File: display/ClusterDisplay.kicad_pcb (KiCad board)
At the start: 4 copper layers, 115.6 x 106 mm, 98 parts, among them J1 Verdin iMX95 Hexa 8GB WB IT, J10 RTC coin cell, J2 Phoenix MKDS 1,5/3-5,08 power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, J3 Molex KK-254 22-27-2031 priva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, J4 TST040HDBC-42 panel, J8 Samtec TSW-108-07-G-S JTAG (b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, J9 Samtec TSW-104-07-G-S buttons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, Q1 PMV55ENEA (AEC-Q101, 60V/20V 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, Q2 PMV55ENEA (AEC-Q101, 60V/20V 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, Q3 PMV55ENEA ignition wake pulld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, U1 LM74930-Q1, U2 LM61460-Q1, U3 TLV767-Q1, U4 TCAN1044V-Q1, U6 TPS65131-Q1, U7 TPS61165-Q1

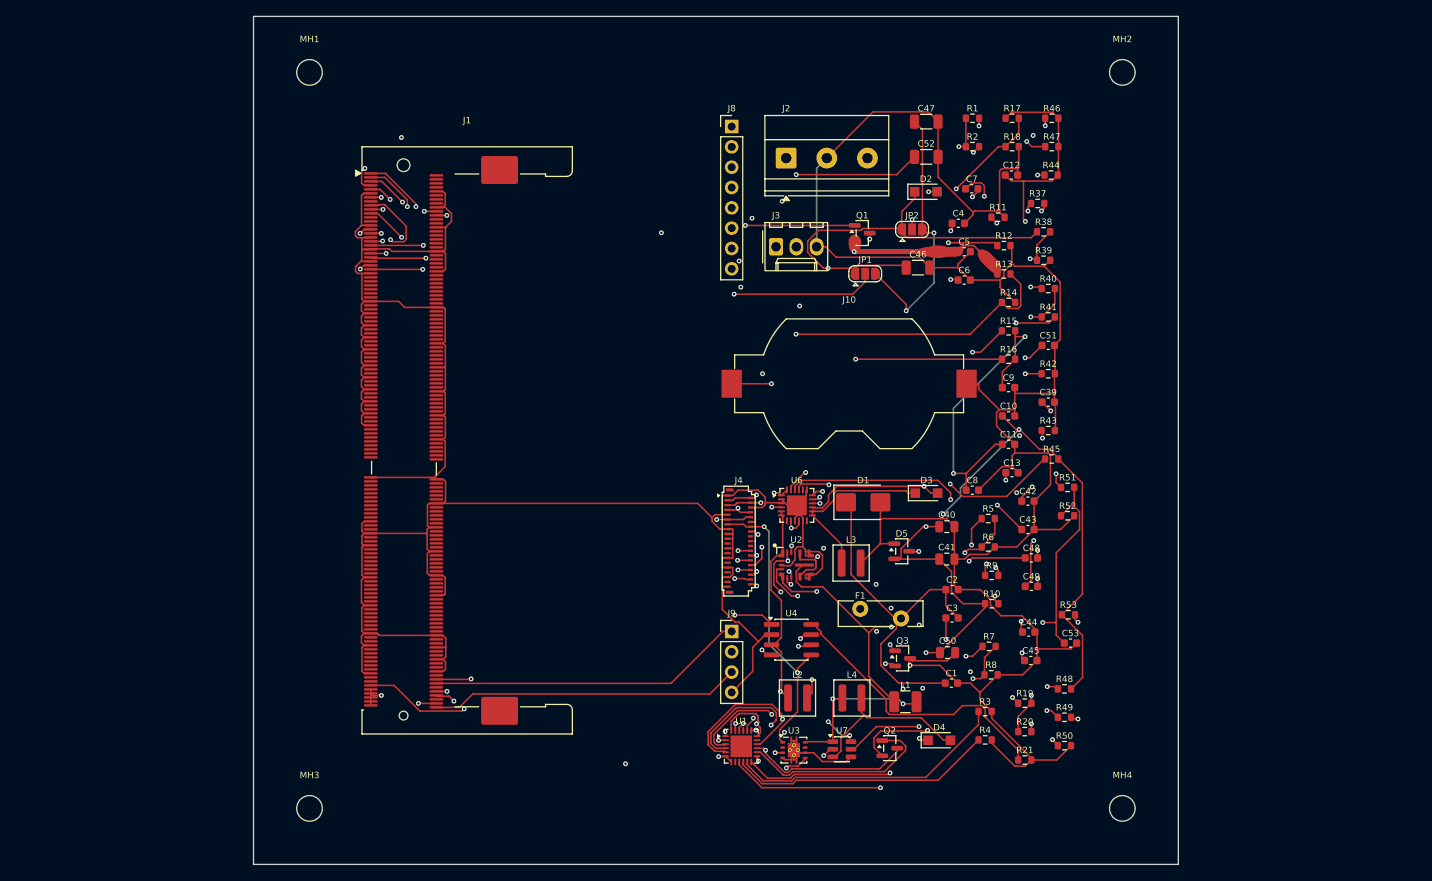
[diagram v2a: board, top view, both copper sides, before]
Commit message: Prepare both boards for fabrication: real power-stage values, orderable BOMs, fab packages
display/ power stage was placeholders inherited from fascia-pcb (RILIM, OV top,
RT, FB top...). Values are now calculated from the LM74930-Q1, LM61460-Q1 and
TLV767-Q1 datasheets, with real packages (1u XEL5030 inductor, 1206 caps, 2 mohm
sense resistor, polymer bulk cap). gauges/ buck inductor (XAL5050, Isat above the
LMR33630 current limit) and input/output capacitors fixed per its datasheet.
tools/passive_catalog.py maps every passive to a real MPN (entries flagged
verified or pattern). fab/build_fab.py writes gerbers, drill, CPL and BOM CSVs
and refuses boards with unconnected nets. Silkscreen text raised to the fab
minimum; gauges input zones moved beside the MCU. Both boards re-routed, 0
unconnected.

Co-Authored-By: Claude Sonnet 5.5 <noreply@anthropic.com>
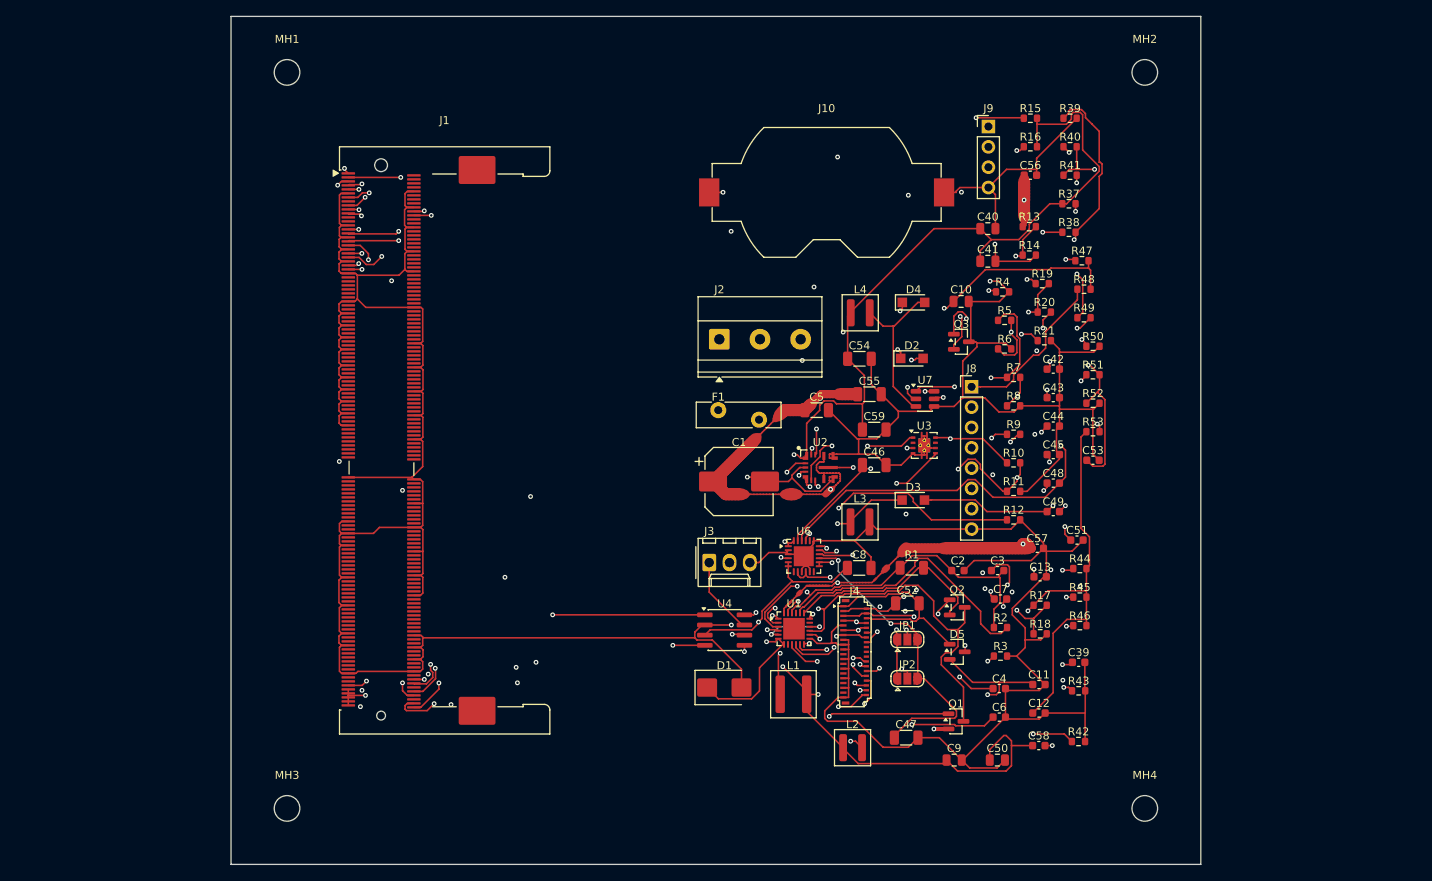
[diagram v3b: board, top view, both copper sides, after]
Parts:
- added C54: 22u COUT, Capacitor_SMD:C_1206_3216Metric, F.Cu at (227.9, 138.3)
- added C55: 4.7u CIN VIN2, Capacitor_SMD:C_1206_3216Metric, F.Cu at (229.2, 142.7)
- added C56: 100n CHF VIN1, Capacitor_SMD:C_0603_1608Metric, F.Cu at (249.3, 115.3)
- added C57: 100n CHF VIN2, Capacitor_SMD:C_0603_1608Metric, F.Cu at (250.2, 162.0)
- added C58: 22p CFF, Capacitor_SMD:C_0603_1608Metric, F.Cu at (250.4, 186.7)
- added C59: 22u COUT, Capacitor_SMD:C_1206_3216Metric, F.Cu at (229.8, 147.2)
- C1: value 100uF -> 100u 35V hybrid polymer hold-up (Panasonic EEH-ZA1V101P); footprint Capacitor_SMD:C_0603_1608Metric -> Capacitor_SMD:CP_Elec_8x10
- C10: value 10u out -> 10u COUT; footprint Capacitor_SMD:C_0603_1608Metric -> Capacitor_SMD:C_0805_2012Metric
- C4: value open CT -> 100n CTMR
- C5: value 10u in -> 4.7u CIN VIN1; footprint Capacitor_SMD:C_0603_1608Metric -> Capacitor_SMD:C_1206_3216Metric
- C52: value 10u BL output 25V (AEC-Q200) -> 4.7u BL output, 50V part (AEC-Q200)
- C8: value 44u out -> 22u COUT; footprint Capacitor_SMD:C_0603_1608Metric -> Capacitor_SMD:C_1206_3216Metric
- C9: value 10u in -> 10u CIN; footprint Capacitor_SMD:C_0603_1608Metric -> Capacitor_SMD:C_0805_2012Metric
- L1: value 2.2u -> 1u XEL5030-102ME 2.1MHz; footprint Inductor_SMD:L_1210_3225Metric -> Inductor_SMD:L_Coilcraft_XAL5030-XXX
- R1: value 2m sense -> 2m 2% sense (Susumu KRL3216E-C-R002-G-T5); footprint Resistor_SMD:R_0603_1608Metric -> Resistor_SMD:R_1206_3216Metric
- R10: value FB top -> 100k FB top
- R11: value FB bot -> 24.9k FB bot
- R12: value RT -> 6.04k RT
- R13: value EN top -> 100k EN top
- R14: value EN bot -> 24.9k EN bot
- R17: value FB top -> 124k FB top
- R18: value FB bot -> 100k FB bot
- R2: value 50R -> 49.9R 1% RSET
- R3: value RILIM -> 60.4k RILIM
- R4: value 5k RMON -> 10k RIMON
- R5: value OV top -> 100k OV top
- R6: value OV bot -> 2.05k OV bot
- R7: value UV top -> 100k UV top
- R8: value UV bot -> 11.5k UV bot
- R9: value RBOOT -> 0R RBOOT
- moved C47 77.1 mm to (233.8, 185.7)
- moved J9 70.8 mm to (244.1, 109.3)
- moved C12 67.3 mm to (250.4, 182.6)
- moved R46 63.5 mm to (255.5, 171.7)
- moved Q1 62.2 mm to (240.0, 183.6)
- moved R18 61.0 mm to (250.5, 172.7)
- moved R17 61.0 mm to (250.5, 169.1)
- moved R2 60.2 mm to (245.6, 171.9)
- moved C4 58.4 mm to (245.4, 179.5)
- moved R1 56.7 mm to (234.5, 164.4)
- moved JP2 56.2 mm to (233.9, 178.3)
- moved R4 56.1 mm to (245.8, 129.9)
- moved C52 55.9 mm to (233.9, 168.9)
- moved D4 54.8 mm to (234.7, 131.2)
- moved C6 54.8 mm to (245.4, 183.1)
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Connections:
- C1 pad 1: VBAT_F -> +12V_PROT
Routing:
- net +5V: track 213.7 -> 333.9 mm, vias 9 -> 8
- net SENSE_OUT: track 111.8 -> 25.7 mm, vias 3 -> 0
- net JTAG_TDI: track 47.1 -> 117.1 mm, vias 1 -> 2
- net +12V_PROT: track 112.3 -> 179.9 mm, vias 3 -> 6
- net TMR: track 94.2 -> 28.5 mm
- net PANEL_BL_LEDA: track 111.5 -> 45.9 mm, vias 4 -> 2
- net CS_PLUS: track 98.9 -> 34.3 mm, vias 3 -> 0
- net JTAG_TCK: track 47.3 -> 108.1 mm, vias 1 -> 2
- net JTAG_TRST: track 48.2 -> 108.7 mm, vias 1 -> 2
- net DSI_D1_P: track 63.7 -> 120.5 mm, vias 2 -> 4
- net FB_1V8: track 97.5 -> 42.6 mm, vias 2 -> 3
- net RECOVERY: track 94.2 -> 148.5 mm, vias 3 -> 2
- net DSI_D0_P: track 63.5 -> 117.4 mm, vias 2 -> 3
- net JTAG_TMS: track 47.7 -> 101.2 mm, vias 1 -> 2
- net DSI_CLK_P: track 63.8 -> 117.2 mm, vias 2 -> 3
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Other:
- board size 115.6 x 106 mm -> 121.2 x 106 mm

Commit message: display: add rotary dial input (J11): 360-degree pot on Verdin ADC_1 plus click on GPIO_1
KK-254 4-pin connector: filtered 1.8V pot supply, wiper through 1k/100nF to ADC_IN0, click with 10k pull-up and
debounce to GPIO_1, BAV99-Q clamps on both external lines. ERC 0 violations, re-routed 0 unconnected, BOM and fab
package regenerated. The dial itself is a companion line still needing a part choice.

Co-Authored-By: Claude Sonnet 5.5 <noreply@anthropic.com>
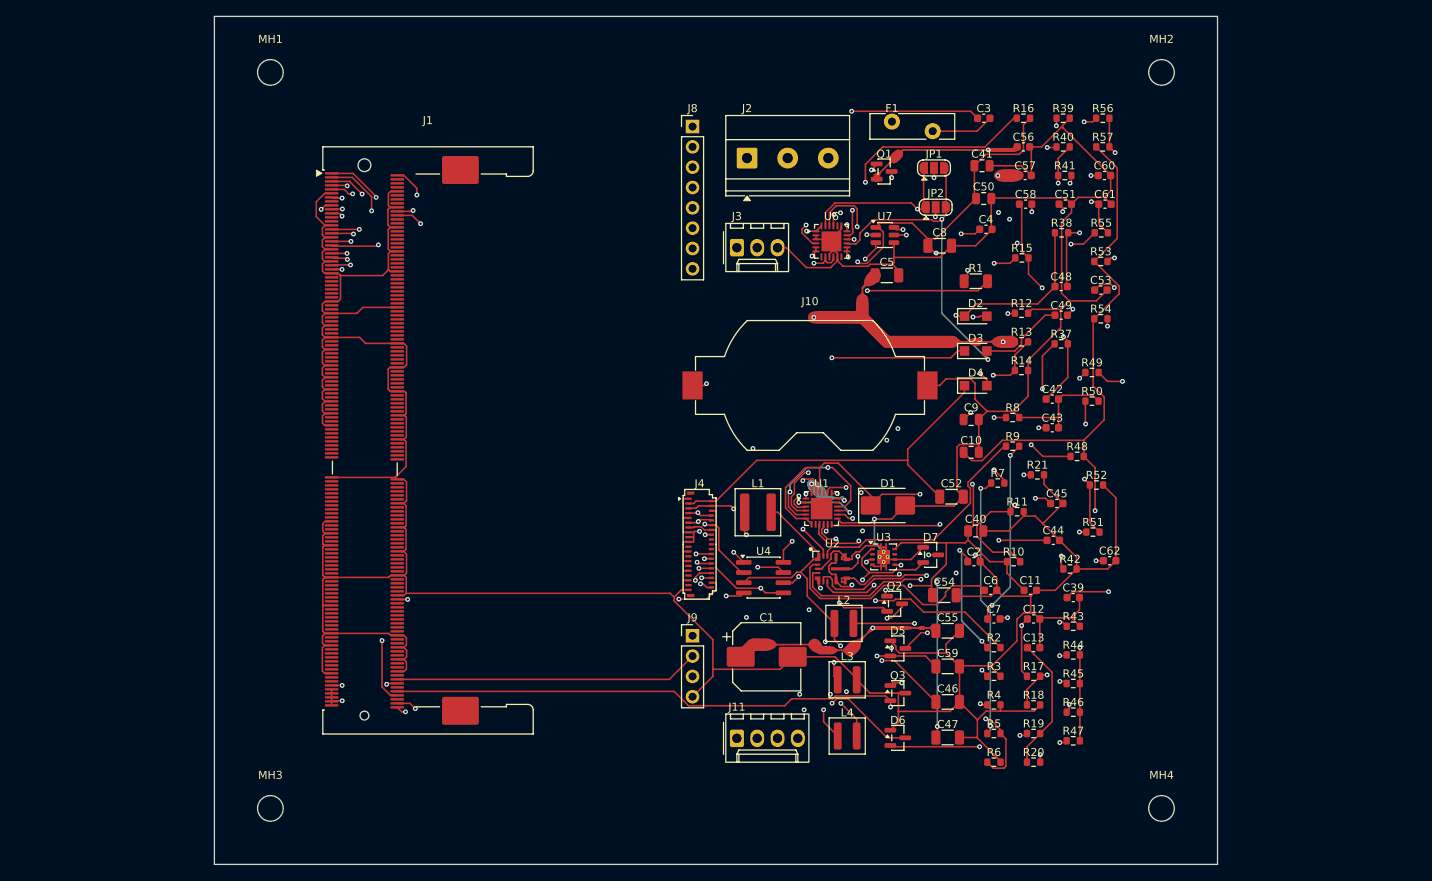
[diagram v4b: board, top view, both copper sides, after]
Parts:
- added C60: 100n dial supply filter, Capacitor_SMD:C_0603_1608Metric, F.Cu at (258.6, 115.4)
- added C61: 100n dial wiper filter, Capacitor_SMD:C_0603_1608Metric, F.Cu at (258.6, 119.0)
- added C62: 100n dial click debounce, Capacitor_SMD:C_0603_1608Metric, F.Cu at (259.2, 163.5)
- added D6: BAV99-Q dial wiper clamp (AEC-Q101), Package_TO_SOT_SMD:SOT-23, F.Cu at (232.7, 185.7)
- added D7: BAV99-Q dial click clamp (AEC-Q101), Package_TO_SOT_SMD:SOT-23, F.Cu at (236.8, 162.8)
- added J11: Molex KK-254 22-27-2041, rotary dial (pot + click), Connector_Molex:Molex_KK-254_AE-6410-04A_1x04_P2.54mm_Vertical, F.Cu at (212.6, 185.7)
- added R54: 100R dial supply series, Resistor_SMD:R_0603_1608Metric, F.Cu at (258.1, 133.3)
- added R55: 1k dial wiper series, Resistor_SMD:R_0603_1608Metric, F.Cu at (258.2, 122.5)
- added R56: 1k dial click series, Resistor_SMD:R_0603_1608Metric, F.Cu at (258.4, 108.2)
- added R57: 10k dial click pull-up to +1V8, Resistor_SMD:R_0603_1608Metric, F.Cu at (258.4, 111.8)
- moved J9 73.6 mm to (207.1, 172.9)
- moved C50 70.2 mm to (243.5, 118.3)
- moved Q1 69.3 mm to (231.0, 114.9)
- moved C58 67.7 mm to (248.7, 119.0)
- moved R47 60.0 mm to (254.7, 186.1)
- moved JP1 59.0 mm to (237.3, 114.4)
- moved JP2 59.0 mm to (237.5, 119.3)
- moved C4 57.4 mm to (243.8, 122.1)
- moved C3 56.6 mm to (243.5, 108.2)
- moved R20 56.3 mm to (249.7, 188.7)
- moved R19 56.3 mm to (249.7, 185.1)
- moved L4 52.9 mm to (226.4, 185.4)
- moved R6 51.7 mm to (244.8, 188.7)
- moved R5 51.7 mm to (244.8, 185.1)
- moved R4 51.6 mm to (244.8, 181.6)
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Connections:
- J1 pad 2: (no net) -> DIAL_ADC
- J1 pad 206: (no net) -> DIAL_CLICK
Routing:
- net DIAL_ADC: track 0.00 -> 169.9 mm, vias 0 -> 4
- net DIAL_CLICK: track 0.00 -> 149.4 mm, vias 0 -> 4
- net DIAL_REF: track 0.00 -> 100.3 mm, vias 0 -> 2
- net DIAL_CLICK_RAW: track 0.00 -> 95.7 mm, vias 0 -> 1
- net DIAL_WIPER: track 0.00 -> 86.7 mm, vias 0 -> 1
- net JTAG_TDI: track 117.1 -> 47.0 mm, vias 2 -> 1
- net BL_SW: track 20.2 -> 88.6 mm, vias 0 -> 3
- net RECOVERY: track 148.5 -> 86.3 mm, vias 2 -> 1
- net PWR_BTN: track 151.7 -> 90.0 mm
- net JTAG_TCK: track 108.1 -> 46.7 mm, vias 2 -> 1
- net JTAG_TRST: track 108.7 -> 48.8 mm, vias 2 -> 1
- net DSI_D0_N: track 121.1 -> 64.3 mm, vias 3 -> 2
- net PANEL_PIN_A: track 11.6 -> 68.0 mm, vias 2 -> 3
- net PANEL_INV_SW: track 16.7 -> 72.5 mm, vias 2 -> 3
- net DSI_D1_P: track 120.5 -> 64.8 mm, vias 4 -> 2
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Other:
- board size 121.2 x 106 mm -> 125.4 x 106 mm

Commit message: display: dial interface for a Piher PSC-360 (switched 5V, scaled analog signal) plus separate click input
PSC-360 is a contactless Hall angle sensor with endless rotation; its switch output is an angle
threshold, not a push button, so J11 keeps a separate click input. Sensor 5V comes through a
TPS22918-Q1 load switch controlled by the Verdin's CTRL_SLEEP_MOCI# so it is off in suspend; the
0-5.5V ratiometric output is divided to fit the 2.1V ADC limit. ERC 0 violations, routed clean,
BOM lists the stocked PSC360G2-F1A-C0000-ERA360-05K for prototyping.

Co-Authored-By: Claude Sonnet 5.5 <noreply@anthropic.com>
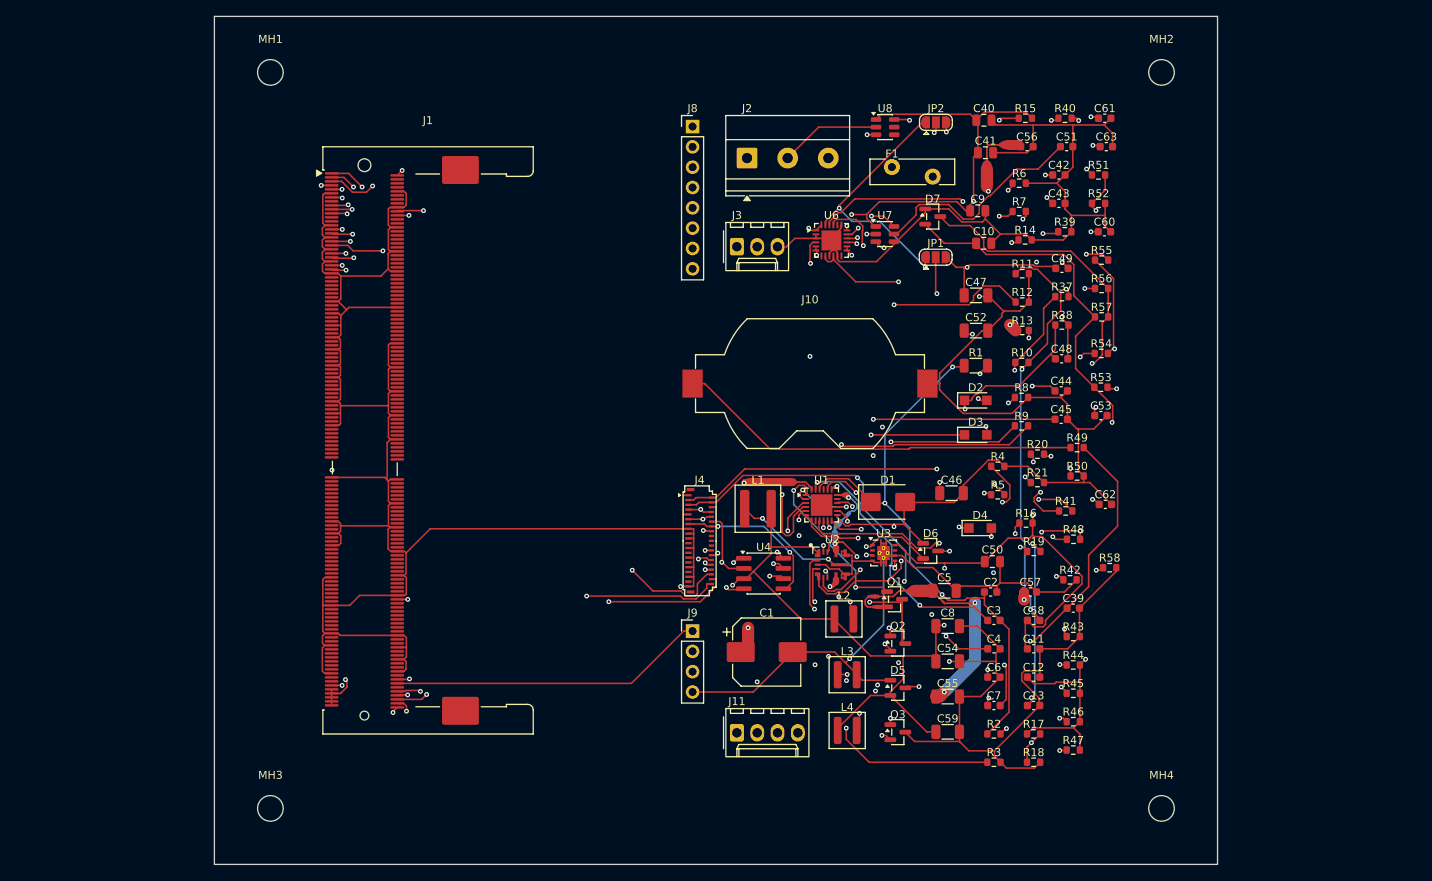
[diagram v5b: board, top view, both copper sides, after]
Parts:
- added C63: 1u dial 5V filter, Capacitor_SMD:C_0603_1608Metric, F.Cu at (258.8, 111.8)
- added R58: 10.2k dial signal divider bottom, Resistor_SMD:R_0603_1608Metric, F.Cu at (259.2, 164.4)
- added U8: TPS22918-Q1 (AEC-Q100 G2) dial 5V switch, Package_TO_SOT_SMD:SOT-23-6, F.Cu at (231.2, 109.3)
- C60: value 100n dial supply filter -> 1u dial switch CIN
- C61: value 100n dial wiper filter -> 100n dial signal filter
- D6: value BAV99-Q dial wiper clamp (AEC-Q101) -> BAV99-Q dial signal clamp (AEC-Q101)
- J11: value Molex KK-254 22-27-2041, rotary dial (pot + click) -> Molex KK-254 22-27-2041, rotary dial (PSC-360 + click)
- R54: value 100R dial supply series -> 22.1k dial signal divider top
- R55: value 1k dial wiper series -> 1k dial signal series
- moved R6 72.4 mm to (247.9, 116.3)
- moved C3 62.8 mm to (244.8, 171.0)
- moved C47 55.4 mm to (242.5, 130.4)
- moved Q1 53.5 mm to (232.3, 168.4)
- moved C4 52.4 mm to (244.8, 174.6)
- moved C57 52.1 mm to (249.3, 167.4)
- moved C58 52.0 mm to (249.7, 171.0)
- moved C40 51.4 mm to (243.5, 108.5)
- moved R16 50.6 mm to (248.8, 158.8)
- moved C8 47.6 mm to (239.0, 171.7)
- moved C50 45.4 mm to (244.6, 163.7)
- moved R51 44.6 mm to (257.8, 115.3)
- moved D7 42.3 mm to (237.1, 120.5)
- moved R41 41.9 mm to (253.7, 157.3)
- moved C5 40.1 mm to (238.6, 167.3)
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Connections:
- C60 pad 1: DIAL_REF -> +5V
- J1 pad 256: (no net) -> SLEEP_MOCI
- J11 pad 1: DIAL_REF -> DIAL_5V
- J11 pad 2: DIAL_WIPER -> DIAL_SIG_RAW
- R54 pad 1: +1V8 -> DIAL_SIG_RAW
- R54 pad 2: DIAL_REF -> DIAL_DIV
- R55 pad 1: DIAL_WIPER -> DIAL_DIV
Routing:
- net SLEEP_MOCI: track 0.00 -> 121.6 mm, vias 0 -> 3
- net DIAL_5V: track 0.00 -> 113.1 mm, vias 0 -> 2
- net DIAL_REF: track 100.3 -> 0.00 mm, vias 2 -> 0
- net DIAL_WIPER: track 86.7 -> 0.00 mm, vias 1 -> 0
- net DIAL_SIG_RAW: track 0.00 -> 86.2 mm, vias 0 -> 2
- net +1V8: track 215.8 -> 168.6 mm, vias 6 -> 7
- net PG_5V: track 78.0 -> 31.7 mm
- net IGN_SENSE: track 78.0 -> 34.0 mm, vias 2 -> 1
- net DIAL_DIV: track 0.00 -> 43.4 mm, vias 0 -> 2
- net COMMON: track 72.5 -> 32.4 mm, vias 4 -> 3
- net CAP_CP: track 68.2 -> 32.8 mm
- net PANEL_VSN: track 122.9 -> 90.4 mm, vias 6 -> 5
- net +5V: track 290.2 -> 322.2 mm, vias 12 -> 10
- net +12V_PROT: track 158.2 -> 190.1 mm, vias 8 -> 11
- net PANEL_VSP: track 115.5 -> 84.1 mm, vias 3 -> 4
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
